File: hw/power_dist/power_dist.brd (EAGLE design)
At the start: 70 x 45 mm, 57 parts, among them J1 JST-ZH6SMT_VERT, J2 JST-PH4SMT_VERT, P1 XT30P, P2 XT30P, P3 XT30P, P4 XT30P, P5 XT30P, P6 XT30P, P7 XT90PW-M, Q1 TPH1R204PL, Q2 TPH1R204PL, Q3 TPH1R204PL, U1 ZXTR2012Z, U2 MAX150628TDFN, U3 STM32G474CEU6, U4 MIC4416, U5 MIC4416, U6 TCAN334G

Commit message: r3 of power_dist
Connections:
- net LED1: now also U3.47; no longer U3.4
- net LED2: now also U3.45; no longer U3.3
- net SWCLK: now also U3.37; no longer U3.38
- net SWDIO: now also U3.36; no longer U3.37
- net VCC: now also U3.1
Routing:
- net SWDIO: track 33.3 -> 44.7 mm
- net LED1: track 9.82 -> 7.40 mm
- net LED2: track 9.08 -> 7.08 mm
- net VCC: track 21.4 -> 22.4 mm, vias 21 -> 22
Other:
- board text added: "moteus power distribution r3"
- board text removed: "moteus power distribution r2"
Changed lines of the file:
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@@
 <wire x1="0" y1="45" x2="0" y2="0" width="0" layer="20"/>
 <text x="27.8" y="22.4" size="1" layer="21" font="vector">moteus
-power distribution r2</text>
+power distribution r3</text>
 <text x="27.8" y="19" size="0.8" layer="21" font="vector" ratio="10">(c) 2019</text>
 <text x="27.8" y="20.8" size="0.8" layer="21" font="vector" ratio="10">jjp@pobox.com</text>
@@
 <wire x1="46.45" y1="10.75" x2="46.45" y2="9.4" width="0.3048" layer="1"/>
 <wire x1="46.45" y1="9.4" x2="46.65" y2="9.4" width="0.3048" layer="1"/>
+<contactref element="U3" pad="1"/>
+<via x="47" y="18.6" extent="1-16" drill="0.3048"/>
+<wire x1="46.95" y1="17.65" x2="47" y2="17.65" width="0.254" layer="1"/>
+<wire x1="47" y1="17.65" x2="47" y2="18.6" width="0.254" layer="1"/>
 </signal>
 <signal name="N$1">
@@
 <signal name="SWDIO">
 <contactref element="J1" pad="3"/>
+<contactref element="U3" pad="36"/>
+<wire x1="49.1" y1="10.7" x2="47" y2="10.7" width="0.127" layer="1"/>
+<wire x1="51.7" y1="8.1" x2="49.1" y2="10.7" width="0.127" layer="1"/>
+<wire x1="52.1" y1="8.1" x2="51.7" y2="8.1" width="0.127" layer="1"/>
+<wire x1="52.1" y1="2.9" x2="52.1" y2="8.1" width="0.127" layer="1"/>
+<wire x1="52.9" y1="2.1" x2="52.1" y2="2.9" width="0.127" layer="1"/>
+<wire x1="54.7" y1="2.1" x2="52.9" y2="2.1" width="0.127" layer="1"/>
+<wire x1="54.7" y1="8" x2="54.7" y2="2.1" width="0.127" layer="1"/>
+<wire x1="55.7" y1="9" x2="54.7" y2="8" width="0.127" layer="1"/>
+<wire x1="68.7" y1="9" x2="55.7" y2="9" width="0.127" layer="1"/>
+<wire x1="68.7" y1="15.4" x2="68.7" y2="9" width="0.127" layer="1"/>
+<wire x1="67.6" y1="16.5" x2="68.7" y2="15.4" width="0.127" layer="1"/>
+<wire x1="65.6" y1="16.5" x2="67.6" y2="16.5" width="0.127" layer="1"/>
+<wire x1="47" y1="10.7" x2="46.95" y2="10.75" width="0.127" layer="1"/>
+<wire x1="65.6" y1="16.5" x2="65.6" y2="16.55" width="0.127" layer="1"/>
+</signal>
+<signal name="SWCLK">
+<contactref element="J1" pad="5"/>
 <contactref element="U3" pad="37"/>
 <wire x1="49.1" y1="11.5" x2="47.7" y2="11.5" width="0.127" layer="1"/>
 <wire x1="49.2" y1="11.6" x2="49.1" y2="11.5" width="0.127" layer="1"/>
-<wire x1="53" y1="11.6" x2="49.2" y2="11.6" width="0.127" layer="1"/>
-<wire x1="53" y1="9.7" x2="53" y2="11.6" width="0.127" layer="1"/>
-<wire x1="53.7" y1="9" x2="53" y2="9.7" width="0.127" layer="1"/>
-<wire x1="68.7" y1="9" x2="53.7" y2="9" width="0.127" layer="1"/>
-<wire x1="68.7" y1="15.4" x2="68.7" y2="9" width="0.127" layer="1"/>
-<wire x1="67.6" y1="16.5" x2="68.7" y2="15.4" width="0.127" layer="1"/>
-<wire x1="65.6" y1="16.5" x2="67.6" y2="16.5" width="0.127" layer="1"/>
-<wire x1="47.7" y1="11.5" x2="47.65" y2="11.45" width="0.127" layer="1"/>
-<wire x1="65.6" y1="16.5" x2="65.6" y2="16.55" width="0.127" layer="1"/>
-</signal>
-<signal name="SWCLK">
-<contactref element="J1" pad="5"/>
-<contactref element="U3" pad="38"/>
-<wire x1="53.3" y1="11.9" x2="47.7" y2="11.9" width="0.127" layer="1"/>
-<wire x1="53.3" y1="9.8" x2="53.3" y2="11.9" width="0.127" layer="1"/>
+<wire x1="53.3" y1="11.6" x2="49.2" y2="11.6" width="0.127" layer="1"/>
+<wire x1="53.3" y1="9.8" x2="53.3" y2="11.6" width="0.127" layer="1"/>
 <wire x1="53.5" y1="9.6" x2="53.3" y2="9.8" width="0.127" layer="1"/>
 <wire x1="63.3" y1="9.6" x2="53.5" y2="9.6" width="0.127" layer="1"/>
@@
 <wire x1="64.3" y1="13.5" x2="63.3" y2="12.5" width="0.127" layer="1"/>
 <wire x1="65.6" y1="13.5" x2="64.3" y2="13.5" width="0.127" layer="1"/>
-<wire x1="47.7" y1="11.9" x2="47.65" y2="11.95" width="0.127" layer="1"/>
+<wire x1="47.7" y1="11.5" x2="47.65" y2="11.45" width="0.127" layer="1"/>
 <wire x1="65.6" y1="13.5" x2="65.6" y2="13.55" width="0.127" layer="1"/>
 </signal>
 <signal name="LED1">
 <contactref element="D1" pad="CATHODE"/>
-<contactref element="U3" pad="4"/>
-<wire x1="45.5" y1="19" x2="53.95" y2="19" width="0.127" layer="1"/>
-<wire x1="45.5" y1="17.7" x2="45.5" y2="19" width="0.127" layer="1"/>
-<wire x1="45.5" y1="17.7" x2="45.45" y2="17.65" width="0.127" layer="1"/>
+<contactref element="U3" pad="47"/>
+<wire x1="51.3" y1="16.4" x2="53.9" y2="19" width="0.127" layer="1"/>
+<wire x1="47.7" y1="16.4" x2="51.3" y2="16.4" width="0.127" layer="1"/>
+<wire x1="53.9" y1="19" x2="53.95" y2="19" width="0.127" layer="1"/>
+<wire x1="47.7" y1="16.4" x2="47.65" y2="16.45" width="0.127" layer="1"/>
 </signal>
 <signal name="LED2">
 <contactref element="D2" pad="CATHODE"/>
-<contactref element="U3" pad="3"/>
-<wire x1="51.5" y1="17.2" x2="53.95" y2="17.2" width="0.127" layer="1"/>
-<wire x1="50.4" y1="18.3" x2="51.5" y2="17.2" width="0.127" layer="1"/>
-<wire x1="46" y1="18.3" x2="50.4" y2="18.3" width="0.127" layer="1"/>
-<wire x1="46" y1="17.7" x2="46" y2="18.3" width="0.127" layer="1"/>
-<wire x1="46" y1="17.7" x2="45.95" y2="17.65" width="0.127" layer="1"/>
+<contactref element="U3" pad="45"/>
+<wire x1="52.5" y1="17.2" x2="53.95" y2="17.2" width="0.127" layer="1"/>
+<wire x1="51.1" y1="15.8" x2="52.5" y2="17.2" width="0.127" layer="1"/>
+<wire x1="48.3" y1="15.8" x2="51.1" y2="15.8" width="0.127" layer="1"/>
+<wire x1="48.3" y1="15.7" x2="48.3" y2="15.8" width="0.127" layer="1"/>
+<wire x1="48.1" y1="15.5" x2="48.3" y2="15.7" width="0.127" layer="1"/>
+<wire x1="47.7" y1="15.5" x2="48.1" y2="15.5" width="0.127" layer="1"/>
+<wire x1="47.7" y1="15.5" x2="47.65" y2="15.45" width="0.127" layer="1"/>
 </signal>
 <signal name="CAN_RX">

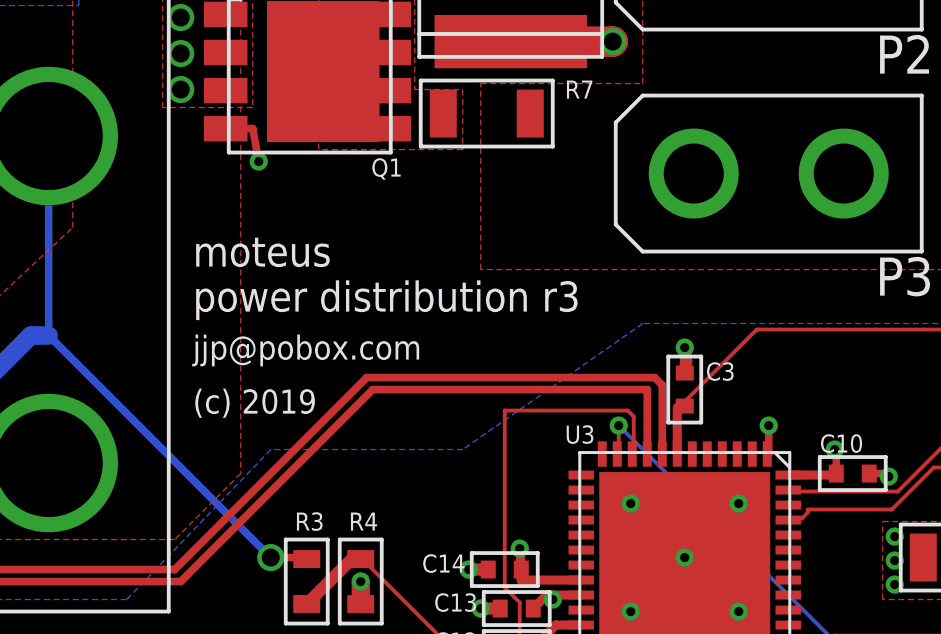
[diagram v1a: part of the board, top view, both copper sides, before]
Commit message: Add mjbots logo to power dist board
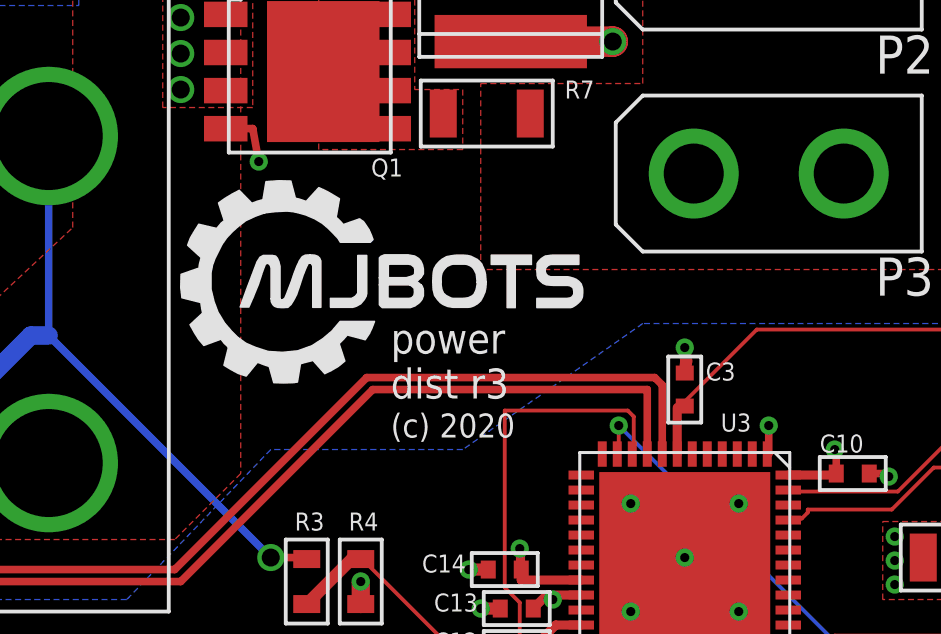
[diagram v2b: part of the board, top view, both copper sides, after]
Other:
- board text added: "(c) 2020"
- board text added: "power dist r3"
- board text removed: "(c) 2019"
- board text removed: "jjp@pobox.com"
- board text removed: "moteus power distribution r3"

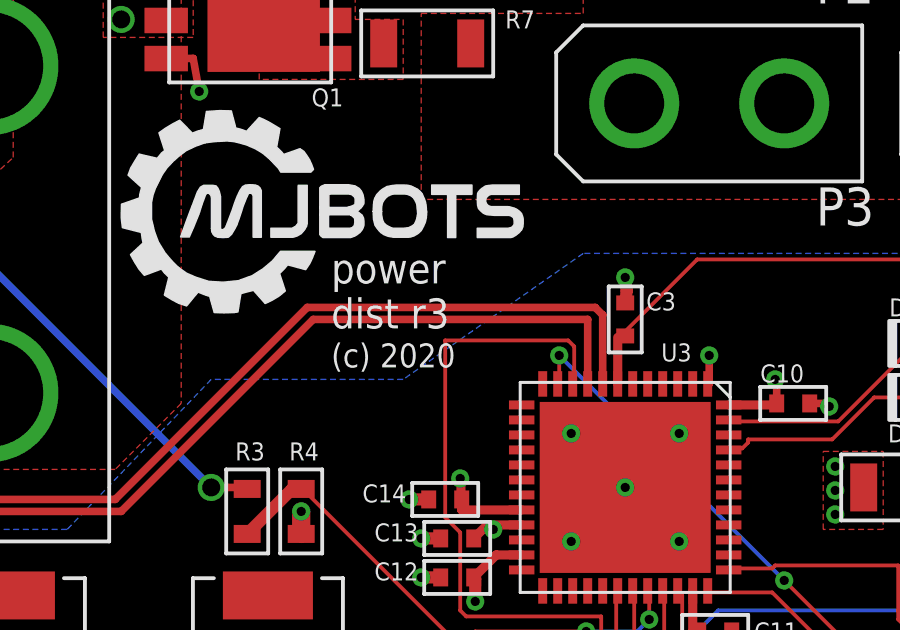
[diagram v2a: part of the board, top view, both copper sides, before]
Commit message: Update power dist to 3.1
The only change is switching out the CAN transceiver for the LTC2875
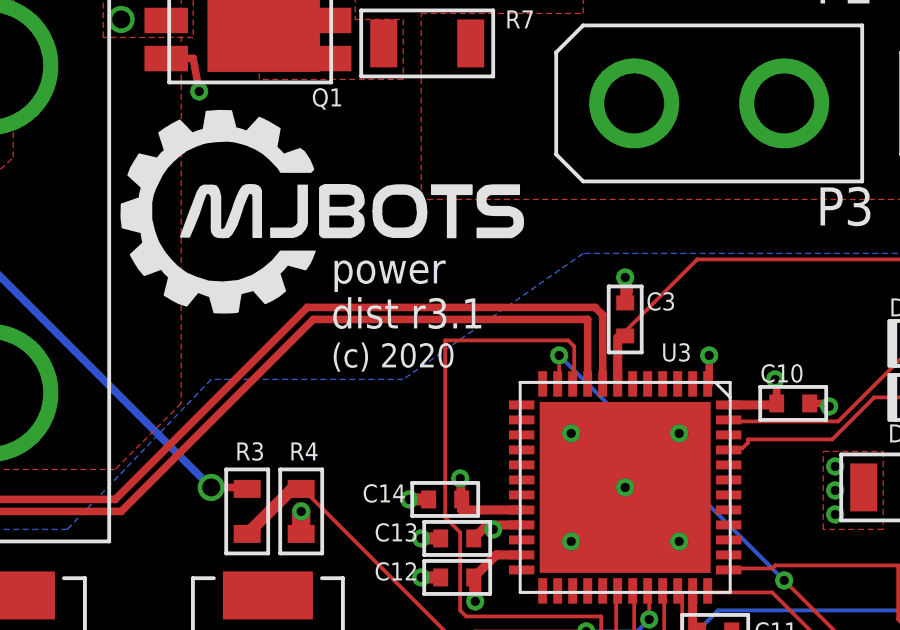
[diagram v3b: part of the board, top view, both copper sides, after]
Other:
- board text added: "power dist r3.1"
- board text removed: "power dist r3"

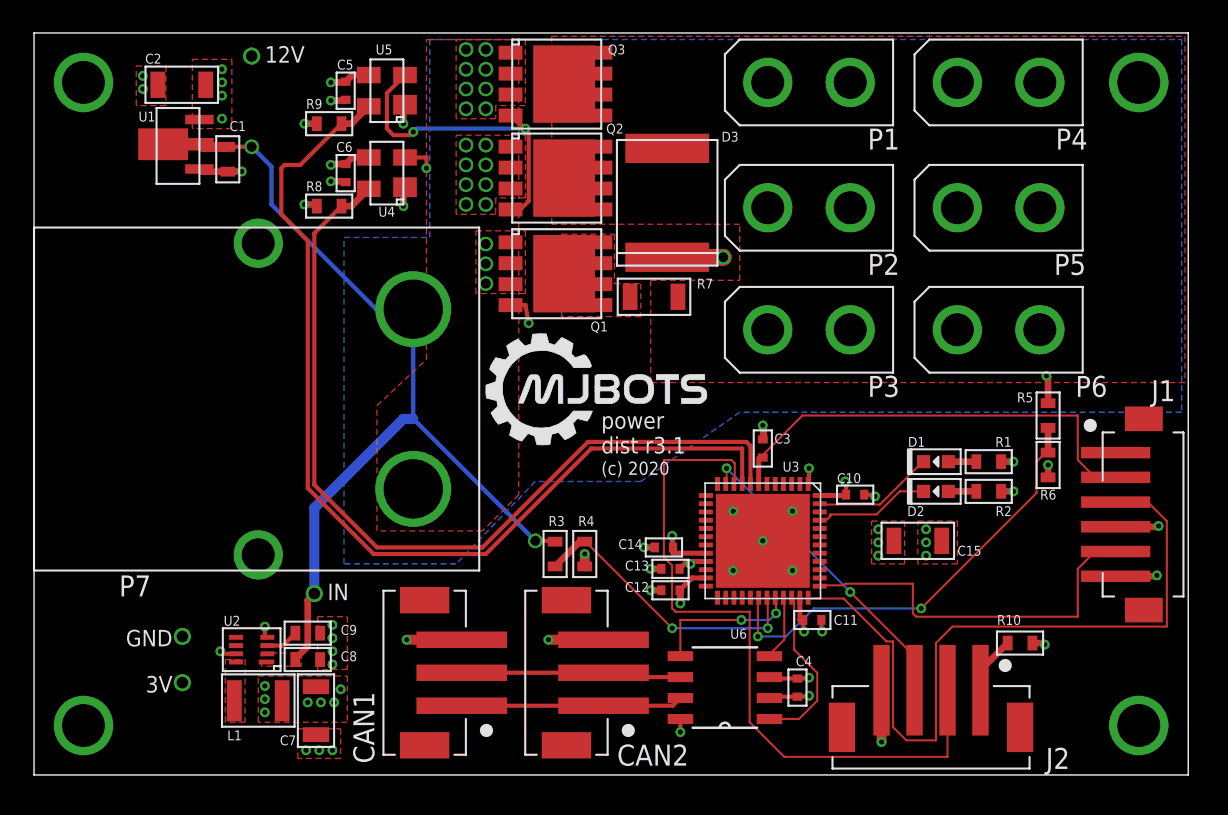
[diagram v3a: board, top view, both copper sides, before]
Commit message: Switch capacitors to soft termination variant
Round corners
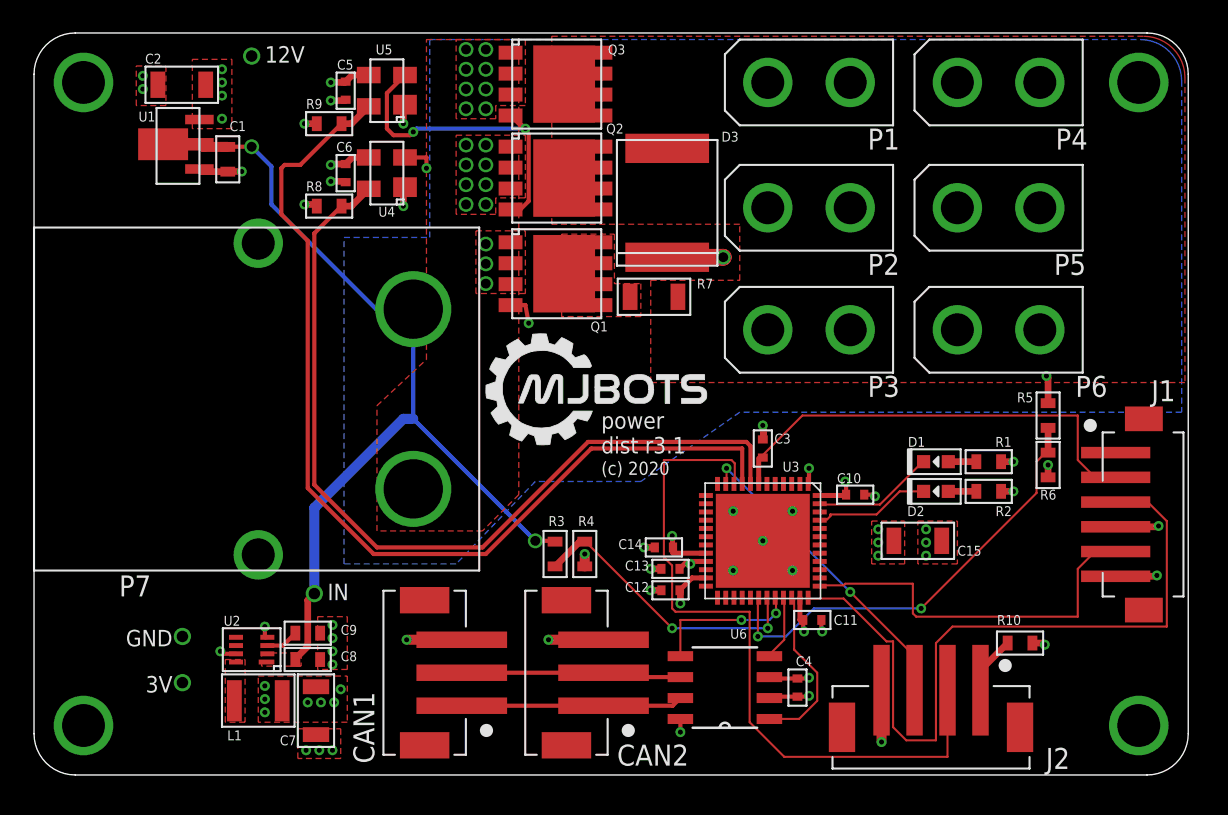
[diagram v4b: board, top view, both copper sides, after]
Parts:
- C15, C2, C7: value 10uF 35V -> 10uF 50V
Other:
- outline, holes or cut-outs redrawn

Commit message: Add some silkscreen labels to power and the switch connector
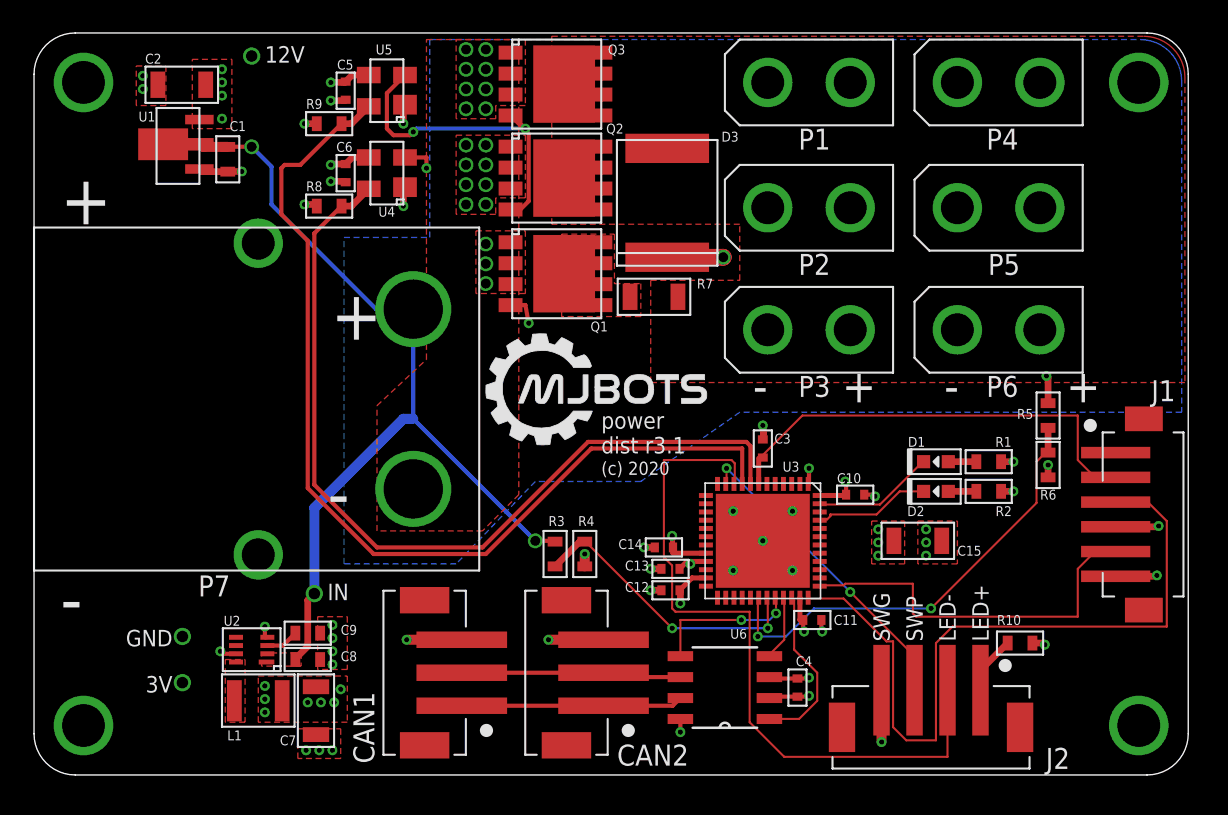
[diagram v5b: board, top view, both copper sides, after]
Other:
- board text added: "+"
- board text added: "-"
- board text added: "LED+"
- board text added: "LED-"
- board text added: "SWG"
- board text added: "SWP"
